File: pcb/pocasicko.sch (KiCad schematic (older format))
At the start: 66 parts, among them J1 SMA, J2 Header_SMD_1x05, J3 FPC24, J4 Header_SMD_1x03, Q1 AO3400A, SW1 RESET, SW2 A, SW3 B, SW4 C, SW5 D, U1 CMWX1ZZABZ-091, U2 BME680, U3 MP28200, U4 LM66100

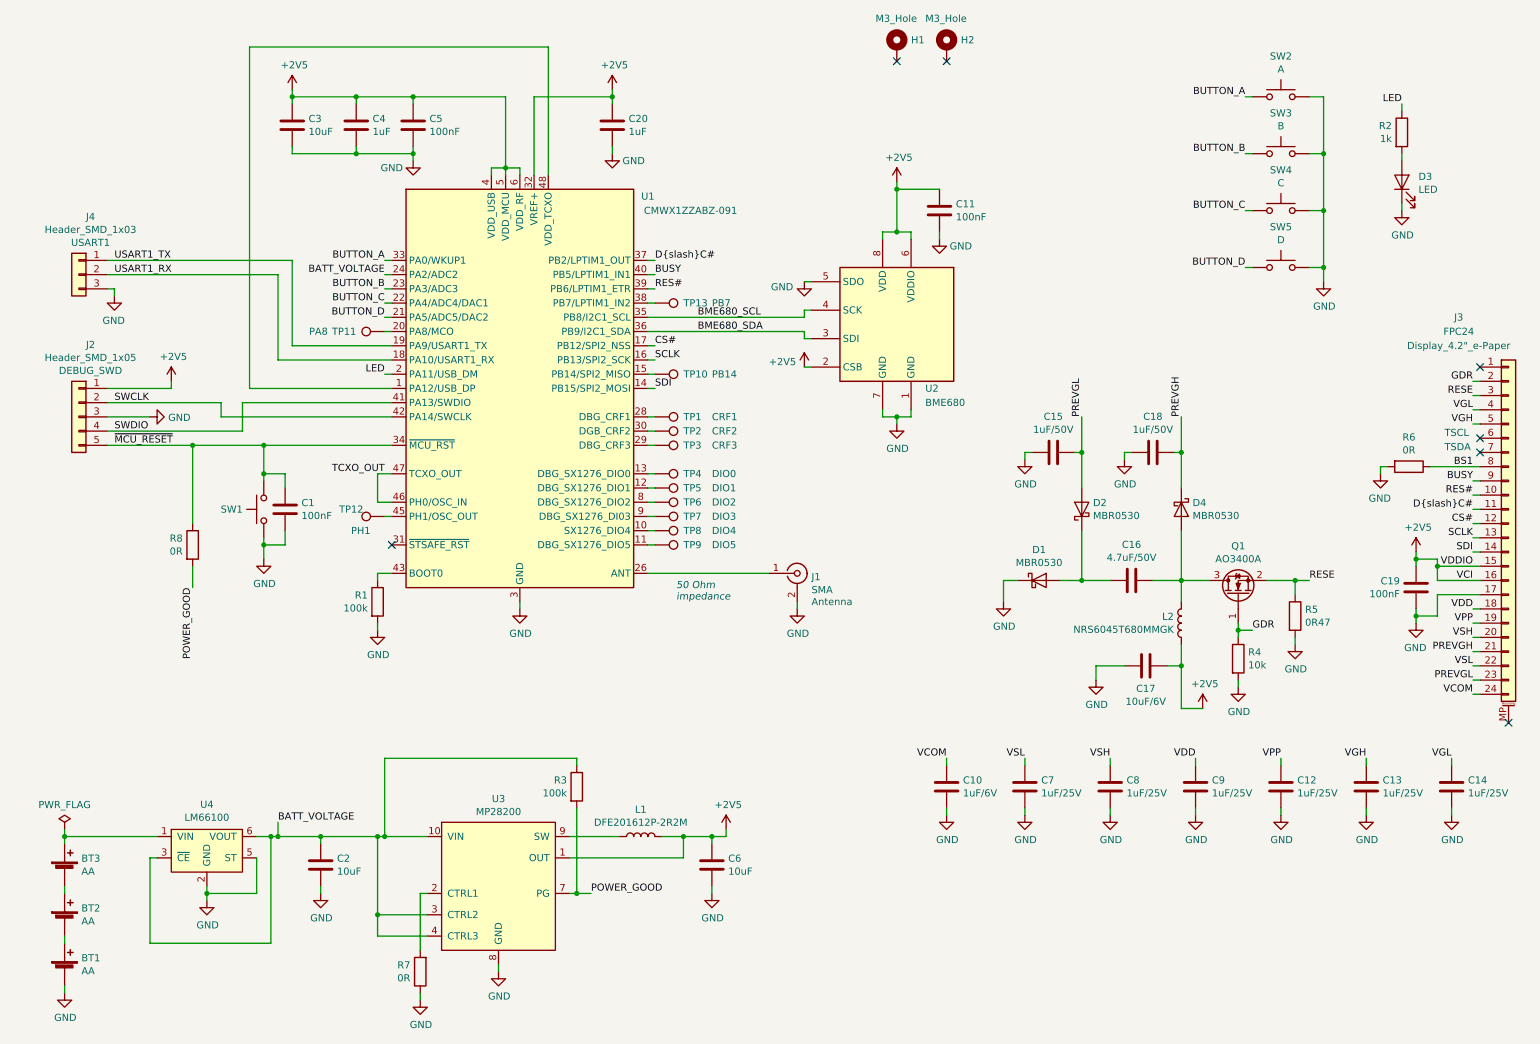
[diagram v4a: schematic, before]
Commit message: Change BME interface from I2C to SPI
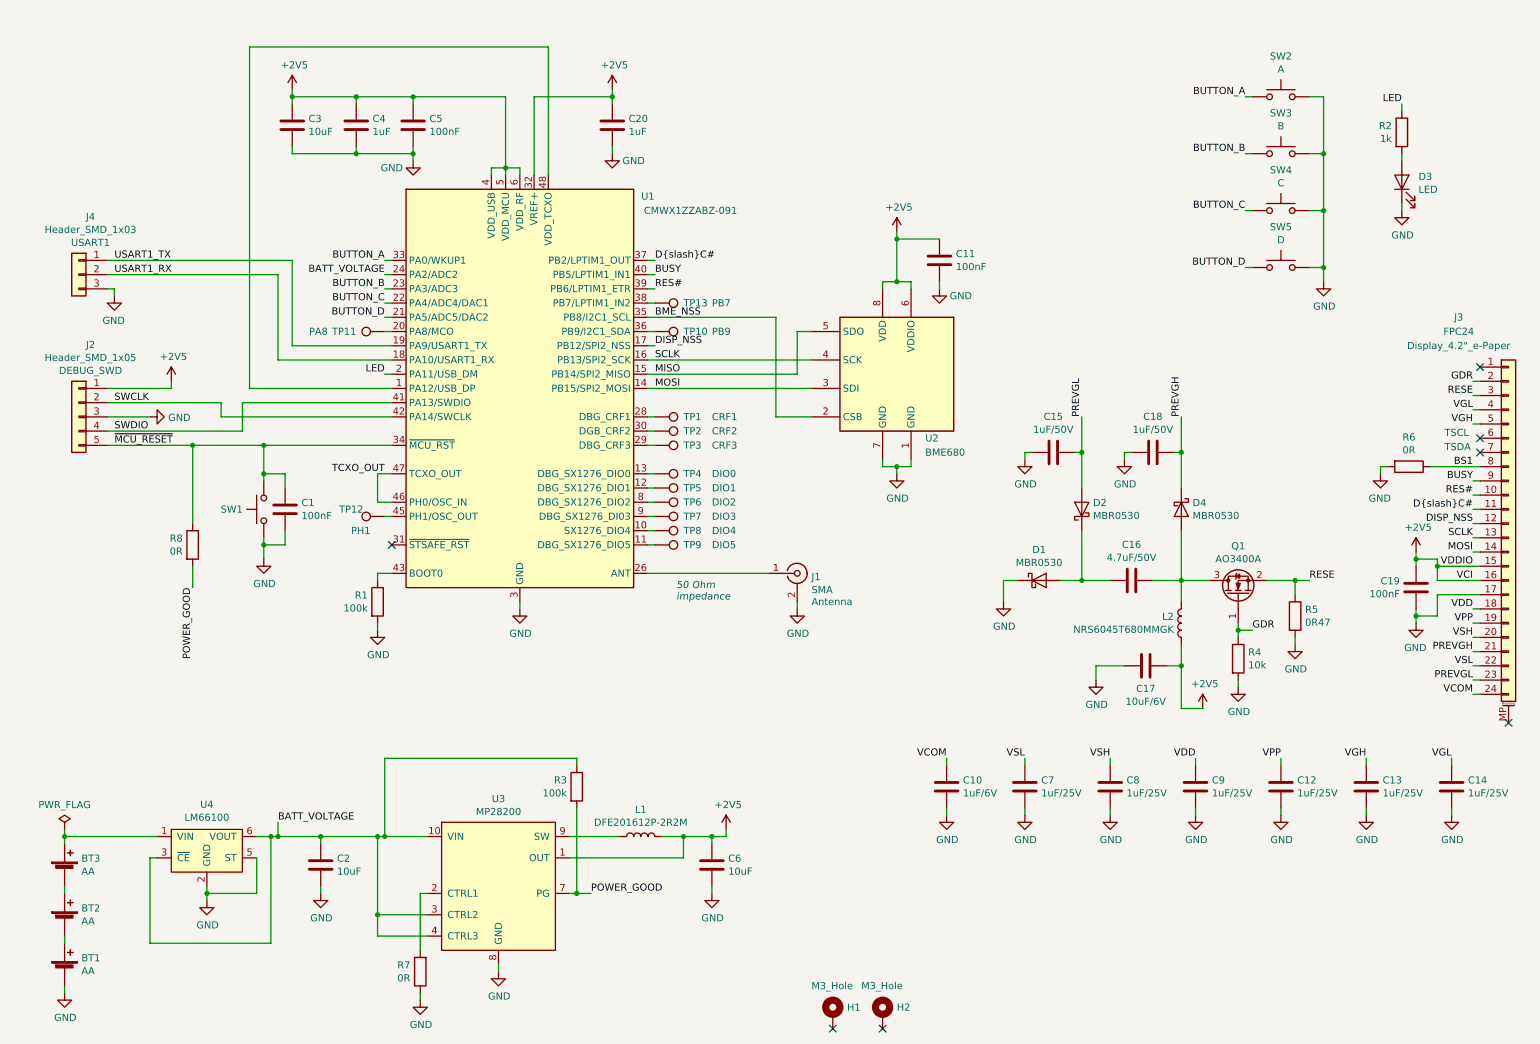
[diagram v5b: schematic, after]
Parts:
- TP10: value PB14 -> PB9
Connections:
- net SDI is gone; now on net MOSI: J3.14 (Pin_14), U1.14 (PB15/SPI2_MOSI)
- net +2V5: no longer U2.2 (CSB)
- net GND: no longer U2.5 (SDO)
- net SCLK: now also U2.4 (SCK)
- net at TP10.1: now also U1.36 (PB9/I2C1_SDA); no longer U1.15 (PB14/SPI2_MISO)
- net BME680_SCL renamed BME_NSS
- net BME_NSS: now also U2.2 (CSB); no longer U2.4 (SCK)
- net BME680_SDA renamed MOSI
- net MOSI: no longer U1.36 (PB9/I2C1_SDA)
- net CS# renamed DISP_NSS
- new net MISO: U1.15 (PB14/SPI2_MISO), U2.5 (SDO)
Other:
- moved on the sheet: C11, H1, H2, U2
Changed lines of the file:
@@
 L power:GND #PWR0104
 U 1 1 5DA410D3
-P 6750 3400
-F 0 "#PWR0104" H 6750 3150 50  0001 C CNN
-F 1 "GND" H 6755 3227 50  0000 C CNN
-F 2 "" H 6750 3400 50  0001 C CNN
-F 3 "" H 6750 3400 50  0001 C CNN
-	1    6750 3400
-	1    0    0    -1
-$EndComp
-Wire Wire Line
-	6650 3300 6650 3350
-Wire Wire Line
-	6650 3350 6750 3350
-Wire Wire Line
-	6750 3350 6750 3400
-Wire Wire Line
-	6750 3350 6850 3350
-Wire Wire Line
-	6850 3350 6850 3300
-Connection ~ 6750 3350
-Wire Wire Line
-	6650 2100 6650 2050
-Wire Wire Line
-	6650 2050 6750 2050
-Wire Wire Line
-	6750 2050 6850 2050
-Wire Wire Line
-	6850 2050 6850 2100
-Connection ~ 6750 2050
+P 6750 3750
+F 0 "#PWR0104" H 6750 3500 50  0001 C CNN
+F 1 "GND" H 6755 3577 50  0000 C CNN
+F 2 "" H 6750 3750 50  0001 C CNN
+F 3 "" H 6750 3750 50  0001 C CNN
+	1    6750 3750
+	1    0    0    -1
+$EndComp
+Wire Wire Line
+	6650 3650 6650 3700
+Wire Wire Line
+	6650 3700 6750 3700
+Wire Wire Line
+	6750 3700 6750 3750
+Wire Wire Line
+	6750 3700 6850 3700
+Wire Wire Line
+	6850 3700 6850 3650
+Connection ~ 6750 3700
+Wire Wire Line
+	6650 2450 6650 2400
+Wire Wire Line
+	6650 2400 6750 2400
+Wire Wire Line
+	6750 2400 6850 2400
+Wire Wire Line
+	6850 2400 6850 2450
+Connection ~ 6750 2400
 $Comp
 L Switch:SW_Push SW2
@@
 L Sensor:BME680 U2
 U 1 1 5DA52ABC
-P 6750 2700
-F 0 "U2" H 6550 2250 50  0000 R CNN
-F 1 "BME680" H 6550 2150 50  0000 R CNN
-F 2 "Package_LGA:Bosch_LGA-8_3x3mm_P0.8mm_ClockwisePinNumbering" H 8200 2250 50  0001 C CNN
-F 3 "https://ae-bst.resource.bosch.com/media/_tech/media/datasheets/BST-BME680-DS001.pdf" H 6750 2500 50  0001 C CNN
-	1    6750 2700
+P 6750 3050
+F 0 "U2" H 6550 2600 50  0000 R CNN
+F 1 "BME680" H 6550 2500 50  0000 R CNN
+F 2 "Package_LGA:Bosch_LGA-8_3x3mm_P0.8mm_ClockwisePinNumbering" H 8200 2600 50  0001 C CNN
+F 3 "https://ae-bst.resource.bosch.com/media/_tech/media/datasheets/BST-BME680-DS001.pdf" H 6750 2850 50  0001 C CNN
+	1    6750 3050
 	-1   0    0    -1
 $EndComp
@@
 Wire Wire Line
 	2300 4200 2300 4250
-$Comp
-L power:GND #PWR0112
-U 1 1 5DA92340
-P 6100 2400
-F 0 "#PWR0112" H 6100 2150 50  0001 C CNN
-F 1 "GND" H 6022 2363 50  0000 R CNN
-F 2 "" H 6100 2400 50  0001 C CNN
-F 3 "" H 6100 2400 50  0001 C CNN
-	1    6100 2400
-	1    0    0    -1
-$EndComp
-Wire Wire Line
-	6150 2400 6100 2400
-Wire Wire Line
-	6150 3000 6100 3000
-Wire Wire Line
-	6100 2650 6100 2600
-Wire Wire Line
-	6100 2600 6150 2600
-Wire Wire Line
-	6100 2750 6100 2800
-Wire Wire Line
-	6100 2800 6150 2800
+Wire Wire Line
+	6150 2750 6050 2750
 Wire Wire Line
 	3900 1650 3900 1600
@@
 L Device:C C11
 U 1 1 5DAB3810
-P 7050 1900
-F 0 "C11" H 6935 1854 50  0000 R CNN
-F 1 "100nF" H 6935 1945 50  0000 R CNN
-F 2 "Capacitor_SMD:C_0805_2012Metric" H 7088 1750 50  0001 C CNN
-F 3 "~" H 7050 1900 50  0001 C CNN
-	1    7050 1900
+P 7050 2250
+F 0 "C11" H 6935 2204 50  0000 R CNN
+F 1 "100nF" H 6935 2295 50  0000 R CNN
+F 2 "Capacitor_SMD:C_0805_2012Metric" H 7088 2100 50  0001 C CNN
+F 3 "~" H 7050 2250 50  0001 C CNN
+	1    7050 2250
 	-1   0    0    1
 $EndComp
@@
 L power:GND #PWR0105
 U 1 1 5DAB4862
-P 7050 2100
-F 0 "#PWR0105" H 7050 1850 50  0001 C CNN
-F 1 "GND" H 7200 2050 50  0000 C CNN
-F 2 "" H 7050 2100 50  0001 C CNN
-F 3 "" H 7050 2100 50  0001 C CNN
-	1    7050 2100
-	1    0    0    -1
-$EndComp
-Wire Wire Line
-	6750 2050 6750 1750
-Connection ~ 6750 1750
-Wire Wire Line
-	6750 1750 6750 1700
-Wire Wire Line
-	7050 2050 7050 2100
-Wire Wire Line
-	7050 1750 6750 1750
+P 7050 2450
+F 0 "#PWR0105" H 7050 2200 50  0001 C CNN
+F 1 "GND" H 7200 2400 50  0000 C CNN
+F 2 "" H 7050 2450 50  0001 C CNN
+F 3 "" H 7050 2450 50  0001 C CNN
+	1    7050 2450
+	1    0    0    -1
+$EndComp
+Wire Wire Line
+	6750 2400 6750 2100
+Connection ~ 6750 2100
+Wire Wire Line
+	6750 2100 6750 2050
+Wire Wire Line
+	7050 2400 7050 2450
+Wire Wire Line
+	7050 2100 6750 2100
 Text Notes 5200 4650 0    50   Italic 0
 50 Ohm\nimpedance
@@
 D{slash}C#
 Text Label 10800 4100 2    50   ~ 0
-CS#
+DISP_NSS
 Text Label 10800 4200 2    50   ~ 0
 SCLK
 Text Label 10800 4300 2    50   ~ 0
-SDI
+MOSI
 Text Label 10800 4400 2    50   ~ 0
 VDDIO
@@
 Wire Wire Line
 	10850 5300 10800 5300
-Text Label 5350 2650 0    50   ~ 0
-BME680_SCL
-Text Label 5350 2750 0    50   ~ 0
-BME680_SDA
 $Comp
 L Device:C C10
@@
 L power:+2V5 #PWR0122
 U 1 1 5DAE1353
-P 6750 1700
-F 0 "#PWR0122" H 6750 1550 50  0001 C CNN
-F 1 "+2V5" H 6765 1873 50  0000 C CNN
-F 2 "" H 6750 1700 50  0001 C CNN
-F 3 "" H 6750 1700 50  0001 C CNN
-	1    6750 1700
+P 6750 2050
+F 0 "#PWR0122" H 6750 1900 50  0001 C CNN
+F 1 "+2V5" H 6765 2223 50  0000 C CNN
+F 2 "" H 6750 2050 50  0001 C CNN
+F 3 "" H 6750 2050 50  0001 C CNN
+	1    6750 2050
 	1    0    0    -1
 $EndComp
@@
 	9550 4900 9550 4950
 Wire Wire Line
-	5000 2650 6100 2650
-Wire Wire Line
-	5000 2750 6100 2750
-Wire Wire Line
 	9550 4500 9650 4500
 Connection ~ 9550 4500
@@
 D{slash}C#
 Text Label 5050 2850 0    50   ~ 0
-CS#
+DISP_NSS
 Text Label 5050 2450 0    50   ~ 0
 RES#
 Text Label 5050 2950 0    50   ~ 0
 SCLK
-Wire Wire Line
-	5000 2950 5050 2950
 Text Label 5050 3150 0    50   ~ 0
-SDI
-Wire Wire Line
-	5000 3150 5050 3150
-Wire Wire Line
-	5000 2850 5050 2850
+MOSI
 Text Label 5050 2350 0    50   ~ 0
 BUSY
@@
 Wire Wire Line
 	10300 1150 10300 1200
-$Comp
-L Connector:TestPoint TP10
-U 1 1 5DB68EB6
-P 5050 3050
-F 0 "TP10" V 5050 3250 50  0000 L CNN
-F 1 "PB14" V 5050 3450 50  0000 L CNN
-F 2 "TestPoint:TestPoint_Pad_D1.0mm" H 5250 3050 50  0001 C CNN
-F 3 "~" H 5250 3050 50  0001 C CNN
-	1    5050 3050
-	0    1    1    0
-$EndComp
-Wire Wire Line
-	5000 3050 5050 3050
 Text Label 9200 1100 2    50   ~ 0
 BUTTON_A
@@
 L Mechanical:MountingHole_Pad H1
 U 1 1 5DB2322A
-P 6750 750
-F 0 "H1" H 6850 799 50  0000 L CNN
-F 1 "M3_Hole" H 6600 950 50  0000 L CNN
-F 2 "MountingHole:MountingHole_3.2mm_M3_DIN965_Pad" H 6750 750 50  0001 C CNN
-F 3 "~" H 6750 750 50  0001 C CNN
-	1    6750 750
+P 6300 7550
+F 0 "H1" H 6400 7599 50  0000 L CNN
+F 1 "M3_Hole" H 6150 7750 50  0000 L CNN
+F 2 "MountingHole:MountingHole_3.2mm_M3_DIN965_Pad" H 6300 7550 50  0001 C CNN
+F 3 "~" H 6300 7550 50  0001 C CNN
+	1    6300 7550
 	1    0    0    -1
 $EndComp
@@
 L Mechanical:MountingHole_Pad H2
 U 1 1 5DB28280
-P 7100 750
-F 0 "H2" H 7200 799 50  0000 L CNN
-F 1 "M3_Hole" H 6950 950 50  0000 L CNN
-F 2 "MountingHole:MountingHole_3.2mm_M3_DIN965_Pad" H 7100 750 50  0001 C CNN
-F 3 "~" H 7100 750 50  0001 C CNN
-	1    7100 750
-	1    0    0    -1
-$EndComp
-NoConn ~ 6750 850
-NoConn ~ 7100 850
+P 6650 7550
+F 0 "H2" H 6750 7599 50  0000 L CNN
+F 1 "M3_Hole" H 6500 7750 50  0000 L CNN
+F 2 "MountingHole:MountingHole_3.2mm_M3_DIN965_Pad" H 6650 7550 50  0001 C CNN
+F 3 "~" H 6650 7550 50  0001 C CNN
+	1    6650 7550
+	1    0    0    -1
+$EndComp
+NoConn ~ 6300 7650
+NoConn ~ 6650 7650
 $Comp
 L Device:C C20
@@
 	4100 1600 4000 1600
 $Comp
-L power:+2V5 #PWR0113
-U 1 1 5DB52717
-P 6100 3000
-F 0 "#PWR0113" H 6100 2850 50  0001 C CNN
-F 1 "+2V5" H 6042 3037 50  0000 R CNN
-F 2 "" H 6100 3000 50  0001 C CNN
-F 3 "" H 6100 3000 50  0001 C CNN
-	1    6100 3000
-	1    0    0    -1
-$EndComp
-$Comp
 L Connector:TestPoint TP11
 U 1 1 5DB8A516
@@
 Text Notes 10600 3600 0    50   ~ 0
 TSDA
+Text Label 5050 3050 0    50   ~ 0
+MISO
+Wire Wire Line
+	5000 2950 6150 2950
+Wire Wire Line
+	5000 3150 6150 3150
+Wire Wire Line
+	5000 3050 6050 3050
+Wire Wire Line
+	6050 3050 6050 2750
+Wire Wire Line
+	5000 2850 5050 2850
+Text Label 5050 2650 0    50   ~ 0
+BME_NSS
+Wire Wire Line
+	5900 2650 5900 3350
+Wire Wire Line
+	5900 3350 6150 3350
+Wire Wire Line
+	5000 2650 5900 2650
+$Comp
+L Connector:TestPoint TP10
+U 1 1 5DB9D4A0
+P 5050 2750
+F 0 "TP10" V 5050 2950 50  0000 L CNN
+F 1 "PB9" V 5050 3150 50  0000 L CNN
+F 2 "TestPoint:TestPoint_Pad_D1.0mm" H 5250 2750 50  0001 C CNN
+F 3 "~" H 5250 2750 50  0001 C CNN
+	1    5050 2750
+	0    1    1    0
+$EndComp
+Wire Wire Line
+	5000 2750 5050 2750
 $EndSCHEMATC
